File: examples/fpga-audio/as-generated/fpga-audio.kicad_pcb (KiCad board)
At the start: 2 copper layers, 100 x 84 mm, 29 parts, among them J1 3V3 IN, J2 AUDIO OUT, J3 SPI PROG, U1 iCE40UP5K, U2 PCM5102A, U3 AP2112K-1.2, U4 W25Q32JV, X1 12MHz

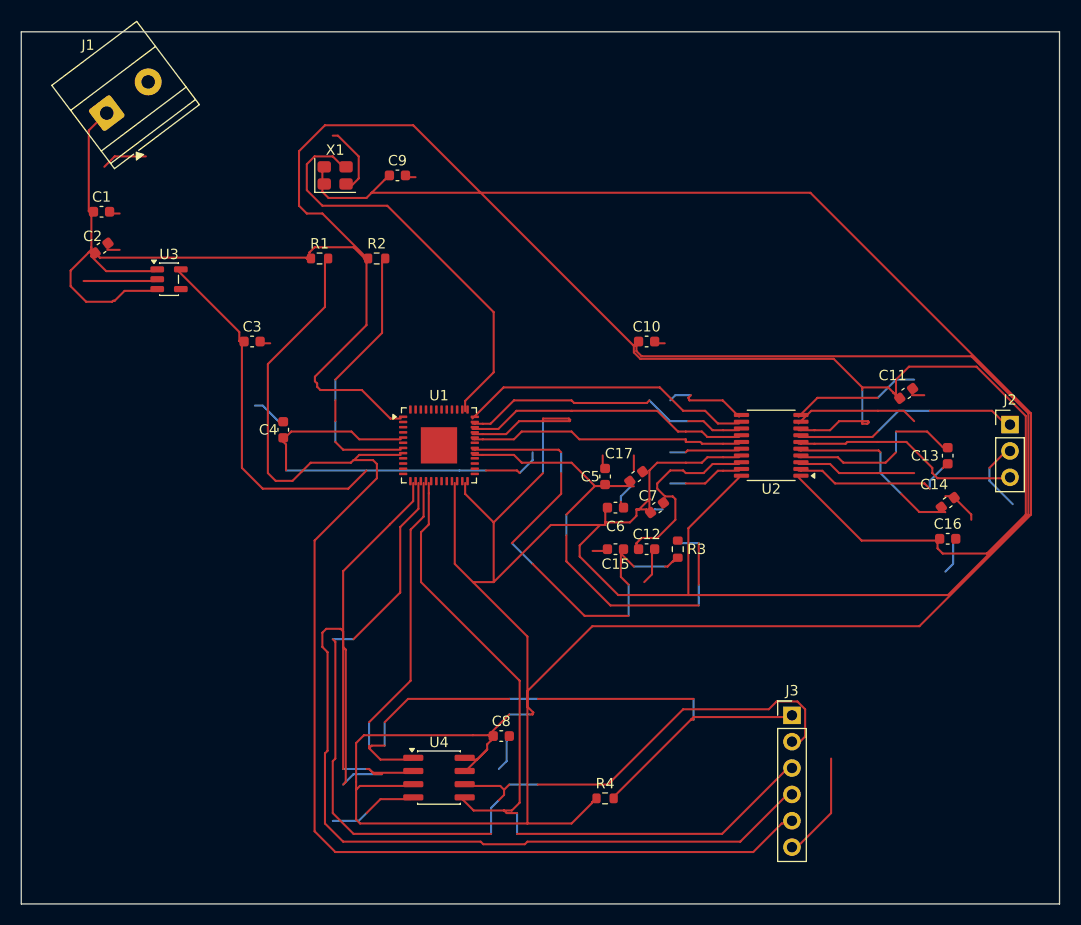
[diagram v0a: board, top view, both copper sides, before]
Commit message: Measure the fold itself, spread it, and keep stitch vias on the board
The reviewer's correction to round thirteen: the circled motor corners
were the bends, not the pour. route.hairpin measures the pair - two
same-direction corners within 1.2 mm summing past 100 degrees, arms of
0.8 mm or more so a via-skirting bump does not count, staircases
cancelling by sign; six findings across the 18 demo projects, info,
promoted only for generated boards. _spread_hairpins answers it by
stretching the fold's middle to 1.2 mm and re-doglegging onto the far
end of the outgoing straight. And stitch-via candidates now stay inside
the pour: offset from a track end, two landed past it - one dead on the
outline - as an edge violation and an orphan at once.

Four boards pass their gates with zero hairpins; the FPGA board's fresh
route is still being drawn.

Co-Authored-By: Claude Fable 5 <noreply@anthropic.com>
Claude-Session: https://claude.ai/code/session_01DUj7Ltu92tWg159mCSacwY
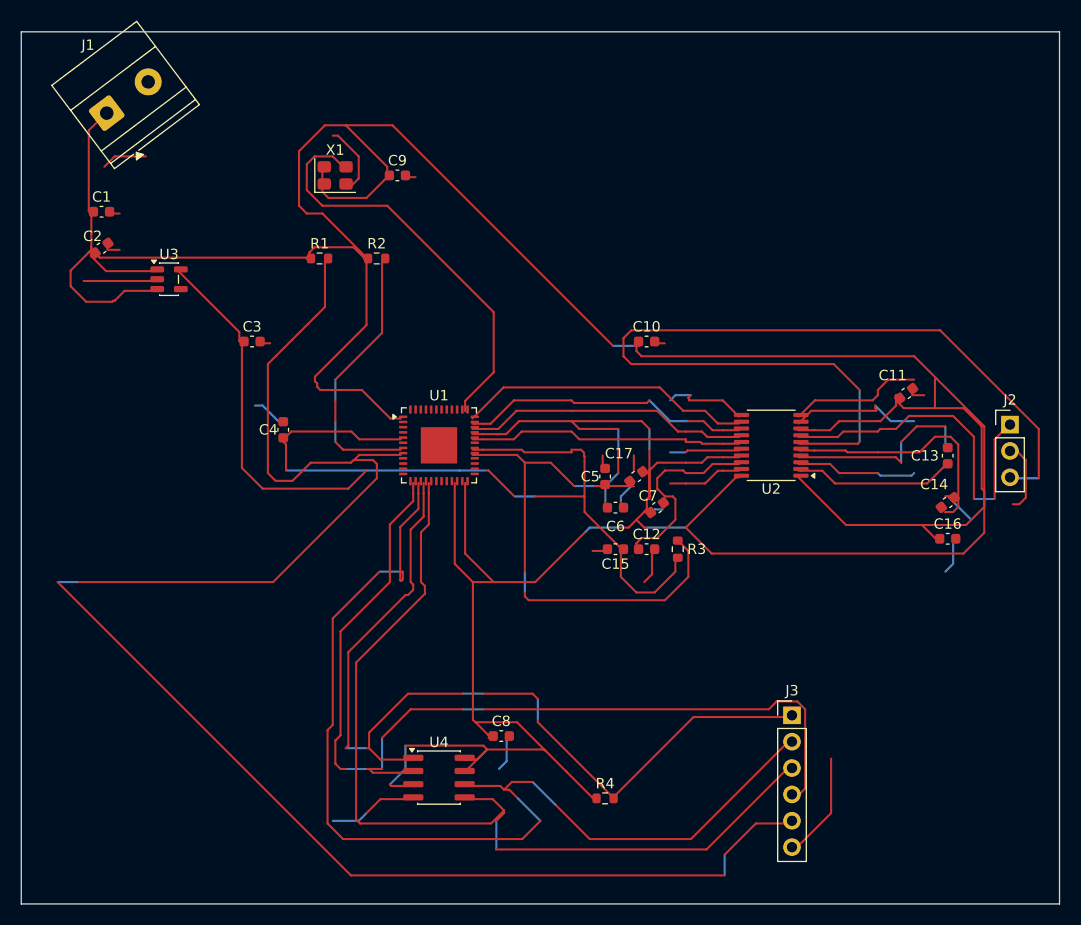
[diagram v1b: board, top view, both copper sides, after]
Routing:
- net +3V3: track 670.7 -> 453.2 mm
- net /OUTL: track 22.0 -> 88.8 mm
- net /CRESET: track 124.9 -> 161.1 mm
- net /SPI_SO: track 126.1 -> 94.0 mm
- net /SPI_SI: track 73.6 -> 90.6 mm
- net /OUTR: track 21.8 -> 34.1 mm
- net /+1V2: track 121.9 -> 112.7 mm
- net /VNEG: track 17.8 -> 23.9 mm
- net /SPI_SCK: track 98.9 -> 104.4 mm
- net /VCCPLL: track 48.0 -> 50.6 mm
- net /CAPM: track 17.5 -> 19.2 mm
- net GND: track 135.4 -> 136.8 mm
- net /SPI_SS: track 89.5 -> 88.3 mm
- net /CAPP: track 16.2 -> 15.4 mm

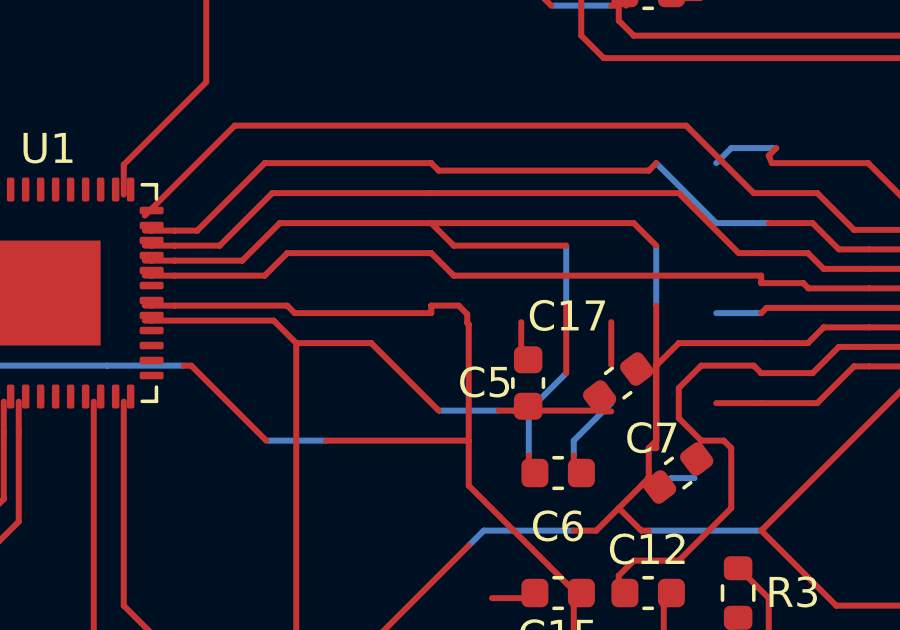
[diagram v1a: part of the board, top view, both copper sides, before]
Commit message: Regenerate the five on the arc and the restored pour, and write it down
The FPGA board's fresh route reproduced its round-fourteen debt to the
digit - after three independent cold draws that is the floorplan fact the
gate says it is, not luck. All five boards measure zero hairpins, zero
crossings, zero doubled runs; the four fast boards pass their gates.
REVIEW.md section 20 records the arc, the retraction of the tongue
pruning, and where the FPGA board stands.

Co-Authored-By: Claude Fable 5 <noreply@anthropic.com>
Claude-Session: https://claude.ai/code/session_01DUj7Ltu92tWg159mCSacwY
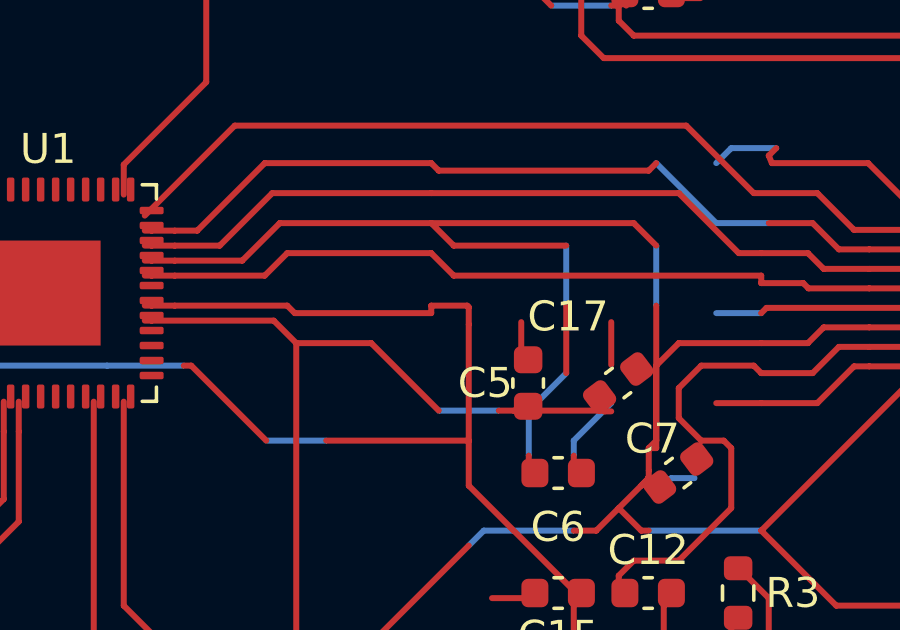
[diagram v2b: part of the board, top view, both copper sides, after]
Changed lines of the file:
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@@
 	(segment (start 148.45 100.5) (end 153.0 100.5) (width 0.2) (layer "F.Cu") (net 2))
 	(segment (start 153.0 100.5) (end 153.0 100.25) (width 0.2) (layer "F.Cu") (net 2))
-	(segment (start 153.0 100.25) (end 153.913 100.25) (width 0.2) (layer "F.Cu") (net 2))
-	(segment (start 153.913 100.25) (end 154.2 100.538) (width 0.2) (layer "F.Cu") (net 2))
-	(segment (start 154.2 100.538) (end 154.2 100.825) (width 0.2) (layer "F.Cu") (net 2))
-	(segment (start 154.2 100.825) (end 154.25 100.875) (width 0.2) (layer "F.Cu") (net 2))
+	(segment (start 153.0 100.25) (end 154.2 100.25) (width 0.2) (layer "F.Cu") (net 2))
+	(segment (start 154.2 100.25) (end 154.25 100.3) (width 0.2) (layer "F.Cu") (net 2))
+	(segment (start 154.25 100.3) (end 154.25 100.875) (width 0.2) (layer "F.Cu") (net 2))
 	(segment (start 154.25 100.875) (end 154.25 104.75) (width 0.2) (layer "F.Cu") (net 2))
 	(segment (start 143.45 100.75) (end 143.68 100.75) (width 0.2) (layer "F.Cu") (net 20))

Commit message: Start the turn at the head of the leg, with no stub at all
The reviewer's last correction on the reversal: the bend back to nine
o'clock - the lead stub the arc kept out the old heading - is not part
of the ideal figure. The turn now starts right where the incoming
straight begins, where the escape's own 45 already points the line, so
the trace draws one continuous curve from pad to bus. Two changes make
that fit: lead 0 is tried before any stub, and when the exit leg is too
short to land on without overshooting, the turn carries through the
exit's own 45 and lands on the straight beyond it.

The motor board's two reversals regenerate as equal-legged turns with
no stub; the FPGA board re-routes (the cache was lost to a container
reclaim) and reproduces its documented debt to the digit for a fourth
independent draw. The as-generated gate counts in the examples README
had drifted behind the rule set and are refreshed while the numbers
were being re-measured.

Co-Authored-By: Claude Fable 5 <noreply@anthropic.com>
Claude-Session: https://claude.ai/code/session_01DUj7Ltu92tWg159mCSacwY
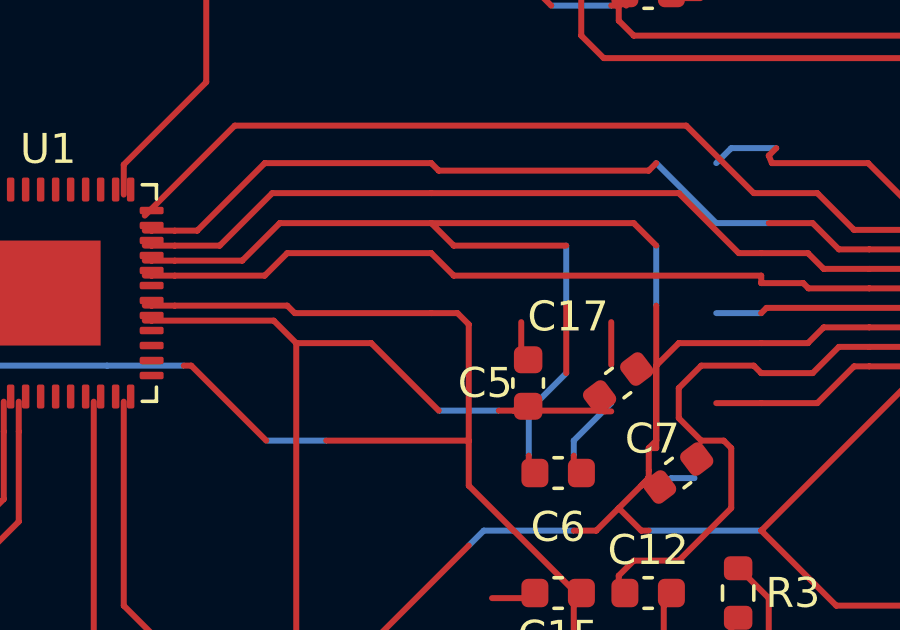
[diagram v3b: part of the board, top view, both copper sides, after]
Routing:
- net /+1V2: track 112.9 -> 112.2 mm
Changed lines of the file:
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@@
 	(segment (start 148.2 100.25) (end 148.45 100.5) (width 0.2) (layer "F.Cu") (net 2))
 	(segment (start 148.45 100.5) (end 153.0 100.5) (width 0.2) (layer "F.Cu") (net 2))
-	(segment (start 153.0 100.5) (end 153.0 100.25) (width 0.2) (layer "F.Cu") (net 2))
-	(segment (start 153.0 100.25) (end 154.2 100.25) (width 0.2) (layer "F.Cu") (net 2))
-	(segment (start 154.2 100.25) (end 154.25 100.3) (width 0.2) (layer "F.Cu") (net 2))
-	(segment (start 154.25 100.3) (end 154.25 100.875) (width 0.2) (layer "F.Cu") (net 2))
+	(segment (start 153.0 100.5) (end 153.875 100.5) (width 0.2) (layer "F.Cu") (net 2))
+	(segment (start 153.875 100.5) (end 154.25 100.875) (width 0.2) (layer "F.Cu") (net 2))
 	(segment (start 154.25 100.875) (end 154.25 104.75) (width 0.2) (layer "F.Cu") (net 2))
 	(segment (start 143.45 100.75) (end 143.68 100.75) (width 0.2) (layer "F.Cu") (net 20))

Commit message: Move the parts out of the corridor, and the tour goes with them
The FPGA board routes again, and better than it did. Letting one track
be promoted more than once before the loop calls its lane impossible was
the last piece: every net that failed had routed on its own when asked,
which is an order to be found rather than a floorplan with none.

Moving the seven parts out from between the two escape fans paid a debt
three rounds old. The line-out tour - 88 mm of copper for a 20 mm net,
`route.detour` and `route.wander` both naming it, reproduced across four
independent cold draws and written down each time as floorplan rather
than routing - is gone; both rules now report nothing. The board's gate
goes from four blocking findings to two, and what is left is the
two-layer bill it has always been: three SPI nets crossing cuts in the
plane, three corners.

Across the five boards: no via sits in a land, DRC is clean on both
matrix versions, and every board keeps zero hairpins, zero crossings and
zero mid-run width steps. The example README's verdict rows are
re-measured, and the guides and REVIEW carry what the ban cost and what
buying it back taught.

Co-Authored-By: Claude Fable 5 <noreply@anthropic.com>
Claude-Session: https://claude.ai/code/session_01DUj7Ltu92tWg159mCSacwY
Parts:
- moved C12 4.00 mm to (160.2, 113.8)
- moved C15 4.00 mm to (157.2, 113.8)
- moved C17 4.00 mm to (159.2, 106.8)
- moved C5 4.00 mm to (156.2, 106.8), turned to 270 degrees
- moved C6 4.00 mm to (157.2, 109.8)
- moved C7 4.00 mm to (161.2, 109.8)
- moved R3 4.00 mm to (163.2, 113.8)
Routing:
- net /OUTL: track 88.8 -> 22.1 mm
- net +3V3: track 453.2 -> 509.2 mm
- net /SPI_SCK: track 104.4 -> 84.5 mm
- net /SPI_SS: track 88.3 -> 107.5 mm
- net /SPI_SI: track 90.6 -> 75.5 mm
- net /OUTR: track 34.1 -> 20.6 mm
- net GND: track 136.8 -> 126.2 mm
- net /VNEG: track 23.9 -> 16.6 mm
- net /LDOO: track 19.3 -> 23.9 mm
- net /CAPM: track 19.2 -> 14.9 mm
- net /CRESET: track 161.1 -> 165.0 mm
- net /+1V2: track 112.2 -> 108.4 mm
- net /VCCPLL: track 50.6 -> 47.1 mm
- net /SPI_SO: track 94.0 -> 96.4 mm
- net /CAPP: track 15.4 -> 17.7 mm

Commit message: Let KiCad fill the plane, and check the fill we actually ship
The reviewer saw copper pushing in between an 0603's pads and asked
whether DRC had been run at all. It had, and it was green, and both
things were true because the check and the drawing were looking at
different polygons.

The fill in the file was ours: a sweep of the pour outline with
everything of another net subtracted, written because a note here said
KiCad's own filler needs a display the container has not got. It does
not - `pcbnew`'s `ZONE_FILLER` runs headless in both images, and always
did by the time that note was written. Meanwhile `pcb drc` was passing
`--refill-zones`, so KiCad threw our polygons away and reported on a
fill of its own. Nobody was checking the one that ships, and it had
drifted: copper 0.075 mm from a foreign pad where the rule says 0.25,
and - measured just now with the refill turned off - two hundred pieces
of copper KiCad calls isolated.

So the zone is declared and left empty, and KiCad fills it: clearance,
minimum width and thermal relief all come from the board's own rules
instead of this file's idea of them. And `drc()` no longer refills a
board whose zones are already filled, because that fill is what goes to
the fab and what the plots draw. A board with an unfilled zone is still
refilled - otherwise every pad on that net reads as unconnected and the
report is noise - and `layout.unfilled_zone` says the file is
incomplete.

All five boards regenerate clean on both matrix versions against their
own committed fill: no errors, nothing unconnected, no isolated copper.
The plane no longer reaches between the passives' lands, and every
through-hole ground pad now has the four spokes of a thermal relief, so
an iron can bring the joint up without heating the whole plane.

The parser gains a pad's corner radius while measuring this, because a
roundrect land's bounding box is a quarter of a millimetre away from
where its copper is.

Co-Authored-By: Claude Fable 5 <noreply@anthr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
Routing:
- net /VCCPLL: track 47.1 -> 48.3 mm
- net GND: track 126.2 -> 124.9 mm
